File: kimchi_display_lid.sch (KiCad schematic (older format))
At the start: 44 parts, among them J1 DF40HC(3.5)-60DS, J2 DF40HC(3.5)-60DS, J3 H19C-6S-0.5SH, J4 FH19C-40S-0.5SH(10), J5 USB_A, U1 24C32, U2 AP3019AKTR-G1, U3 TXS0108EPW, U4 LSM6DSRTR, U5 TPD3S014

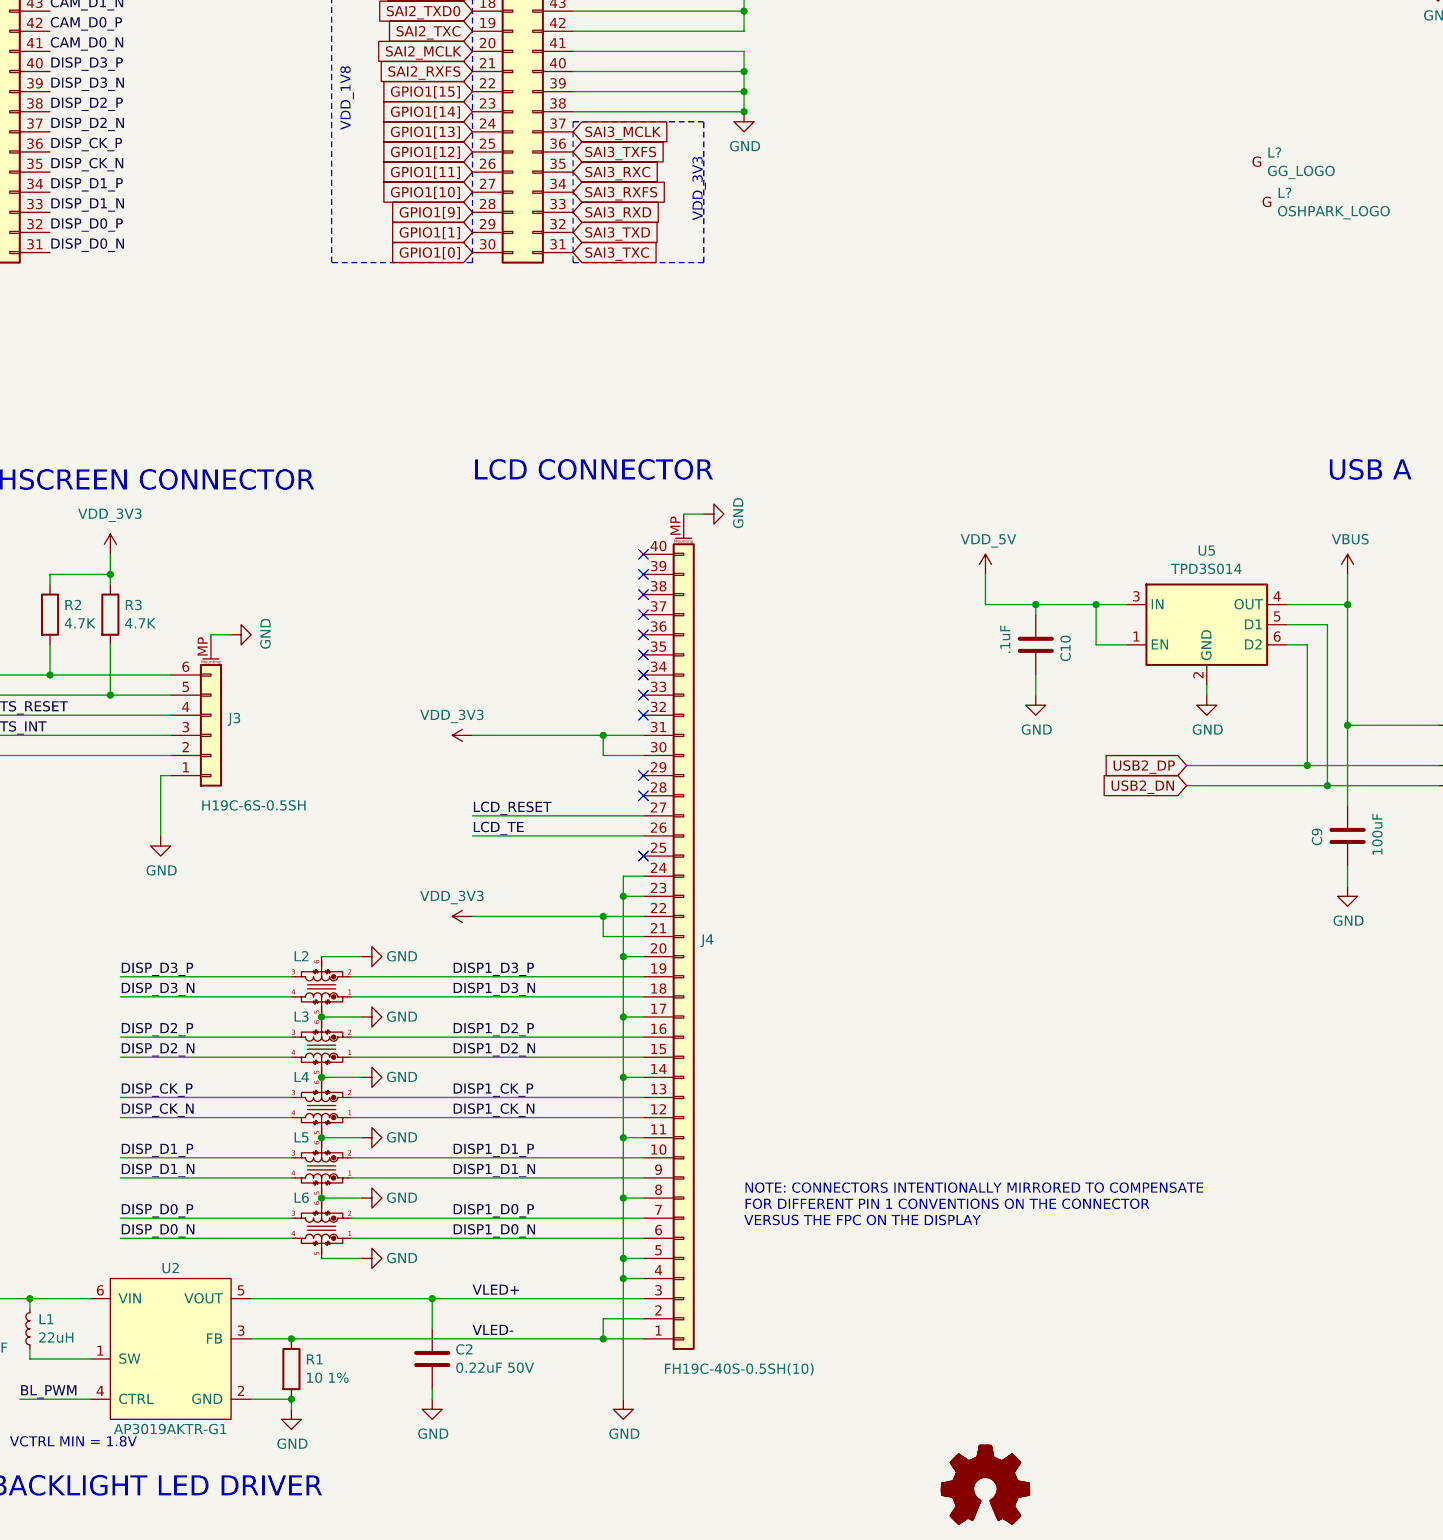
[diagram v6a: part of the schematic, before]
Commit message: Add a small board to connect touchscreen
When the cables wrap around the PCB the distance between
the 40pin and 6pin connectors is too close.

The "hoverboard" floats over the 40pin connector to
air jordan the 6pin down to the main board via a stacked
connector pair.

Signed-off-by: Michael Welling <mwelling@ieee.org>
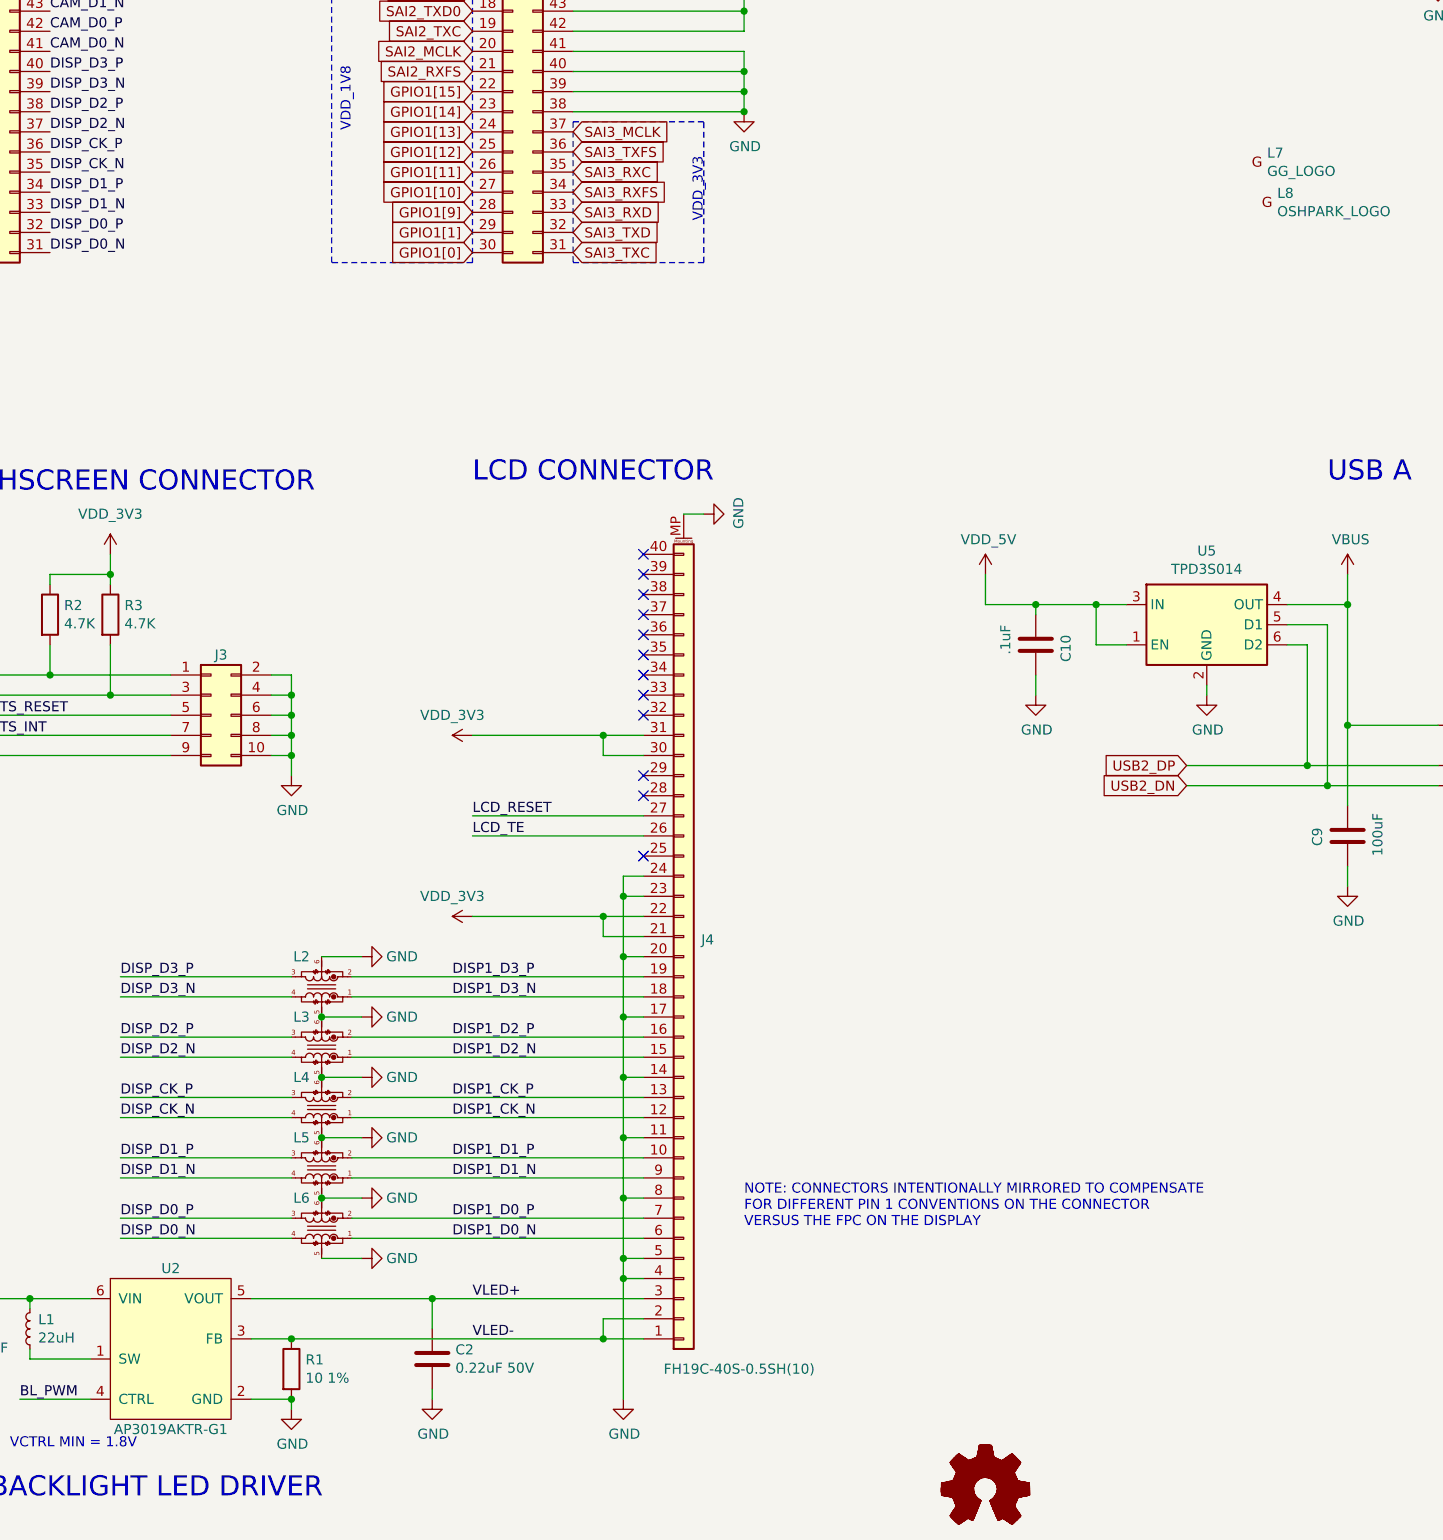
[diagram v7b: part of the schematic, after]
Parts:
- removed J3: H19C-6S-0.5SH, kimchi_ulid:HRS_FH19C-6S-0.5SH_1x06-1MP_P0.50mm, symbol Connector_Generic_MountingPin:Conn_01x06_MountingPin
- added J3: Conn_02x05_Odd_Even, kimchi_ulid:HIROSE_DF23C-10DS-0.5V(51), symbol Connector_Generic:Conn_02x05_Odd_Even
- added LOGO3: Logo_Open_Hardware_Small, kimchi_ulid:hoverboard-3d-model, symbol kimchi_display_lid-rescue:Logo_Open_Hardware_Small-Graphic
- gave numbers to parts that had none: 2
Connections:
- net GND: now also J3.10 (Pin_10), J3.2 (Pin_2), J3.4 (Pin_4), J3.6 (Pin_6), J3.8 (Pin_8)
- net I2C3_SCL: now also J3.3 (Pin_3)
- net I2C3_SDA: now also J3.1 (Pin_1)
- net TS_INT: now also J3.7 (Pin_7)
- net TS_RESET: now also J3.5 (Pin_5)
- net VDD_3V3: now also J3.9 (Pin_9)
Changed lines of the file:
@@
-$EndComp
-$Comp
-L power:GND #PWR0118
-U 1 1 5FD94610
-P 8250 6050
-F 0 "#PWR0118" H 8250 5800 50  0001 C CNN
-F 1 "GND" H 8255 5877 50  0000 C CNN
-F 2 "" H 8250 6050 50  0001 C CNN
-F 3 "" H 8250 6050 50  0001 C CNN
-	1    8250 6050
-	0    -1   -1   0
 $EndComp
 $Comp
@@
 Text Label 7100 6550 0    50   ~ 0
 TS_INT
-$Comp
-L Connector_Generic_MountingPin:Conn_01x06_MountingPin J3
-U 1 1 5FE2A772
-P 8150 6550
-F 0 "J3" H 8237 6466 50  0000 L CNN
-F 1 "H19C-6S-0.5SH" H 8100 6900 50  0000 L CNN
-F 2 "kimchi_ulid:HRS_FH19C-6S-0.5SH_1x06-1MP_P0.50mm" H 8150 6550 50  0001 C CNN
-F 3 "~" H 8150 6550 50  0001 C CNN
-F 4 "H19C-6S-0.5SH" H 8150 6550 50  0001 C CNN "Part"
-	1    8150 6550
-	1    0    0    1
-$EndComp
-Wire Wire Line
-	8150 6050 8250 6050
 Text GLabel 7100 6250 0    50   Input ~ 0
 I2C3_SDA
@@
 L power:GND #PWR0124
 U 1 1 5FE45705
-P 7900 7050
-F 0 "#PWR0124" H 7900 6800 50  0001 C CNN
-F 1 "GND" H 7905 6877 50  0000 C CNN
-F 2 "" H 7900 7050 50  0001 C CNN
-F 3 "" H 7900 7050 50  0001 C CNN
-	1    7900 7050
-	1    0    0    -1
-$EndComp
-Wire Wire Line
-	7950 6750 7900 6750
-Wire Wire Line
-	7900 6750 7900 7050
+P 8550 6750
+F 0 "#PWR0124" H 8550 6500 50  0001 C CNN
+F 1 "GND" H 8555 6577 50  0000 C CNN
+F 2 "" H 8550 6750 50  0001 C CNN
+F 3 "" H 8550 6750 50  0001 C CNN
+	1    8550 6750
+	1    0    0    -1
+$EndComp
 Wire Wire Line
 	9250 9350 10300 9350
@@
 	2350 8850 2350 7400
 $Comp
-L kimchi_ulid:GG_LOGO L?
+L kimchi_ulid:GG_LOGO L7
 U 1 1 601047E2
 P 13350 3700
-F 0 "L?" H 13400 3745 50  0000 L CNN
+F 0 "L7" H 13400 3745 50  0000 L CNN
 F 1 "GG_LOGO" H 13400 3654 50  0000 L CNN
 F 2 "kimchi_ulid:groupgets_logo" H 13350 3700 50  0001 C CNN
@@
 $EndComp
 $Comp
-L kimchi_ulid:OSHPARK_LOGO L?
+L kimchi_ulid:OSHPARK_LOGO L8
 U 1 1 60105FC2
 P 13400 3900
-F 0 "L?" H 13450 3945 50  0000 L CNN
+F 0 "L8" H 13450 3945 50  0000 L CNN
 F 1 "OSHPARK_LOGO" H 13450 3854 50  0000 L CNN
 F 2 "kimchi_ulid:oshpark_logo" H 13400 3900 50  0001 C CNN
@@
 	1    0    0    -1
 $EndComp
+$Comp
+L kimchi_display_lid-rescue:Logo_Open_Hardware_Small-Graphic LOGO3
+U 1 1 601773B5
+P 12000 10300
+F 0 "LOGO3" H 12000 10575 50  0001 C CNN
+F 1 "Logo_Open_Hardware_Small" H 12000 10075 50  0001 C CNN
+F 2 "kimchi_ulid:hoverboard-3d-model" H 12000 10300 50  0001 C CNN
+F 3 "~" H 12000 10300 50  0001 C CNN
+	1    12000 10300
+	1    0    0    -1
+$EndComp
+$Comp
+L Connector_Generic:Conn_02x05_Odd_Even J3
+U 1 1 601AE6C8
+P 8150 6450
+F 0 "J3" H 8200 6750 50  0000 C CNN
+F 1 "Conn_02x05_Odd_Even" H 8200 6776 50  0001 C CNN
+F 2 "kimchi_ulid:HIROSE_DF23C-10DS-0.5V(51)" H 8150 6450 50  0001 C CNN
+F 3 "~" H 8150 6450 50  0001 C CNN
+	1    8150 6450
+	1    0    0    -1
+$EndComp
+Wire Wire Line
+	8450 6250 8550 6250
+Wire Wire Line
+	8550 6250 8550 6350
+Wire Wire Line
+	8450 6650 8550 6650
+Connection ~ 8550 6650
+Wire Wire Line
+	8550 6650 8550 6750
+Wire Wire Line
+	8450 6550 8550 6550
+Connection ~ 8550 6550
+Wire Wire Line
+	8550 6550 8550 6650
+Wire Wire Line
+	8450 6450 8550 6450
+Connection ~ 8550 6450
+Wire Wire Line
+	8550 6450 8550 6550
+Wire Wire Line
+	8450 6350 8550 6350
+Connection ~ 8550 6350
+Wire Wire Line
+	8550 6350 8550 6450
 $EndSCHEMATC
